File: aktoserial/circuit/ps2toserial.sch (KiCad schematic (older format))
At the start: 14 parts, among them IC1 ATMEGA8-P, P1 CONN_4, SW1 SW_PUSH, X1 16MHz

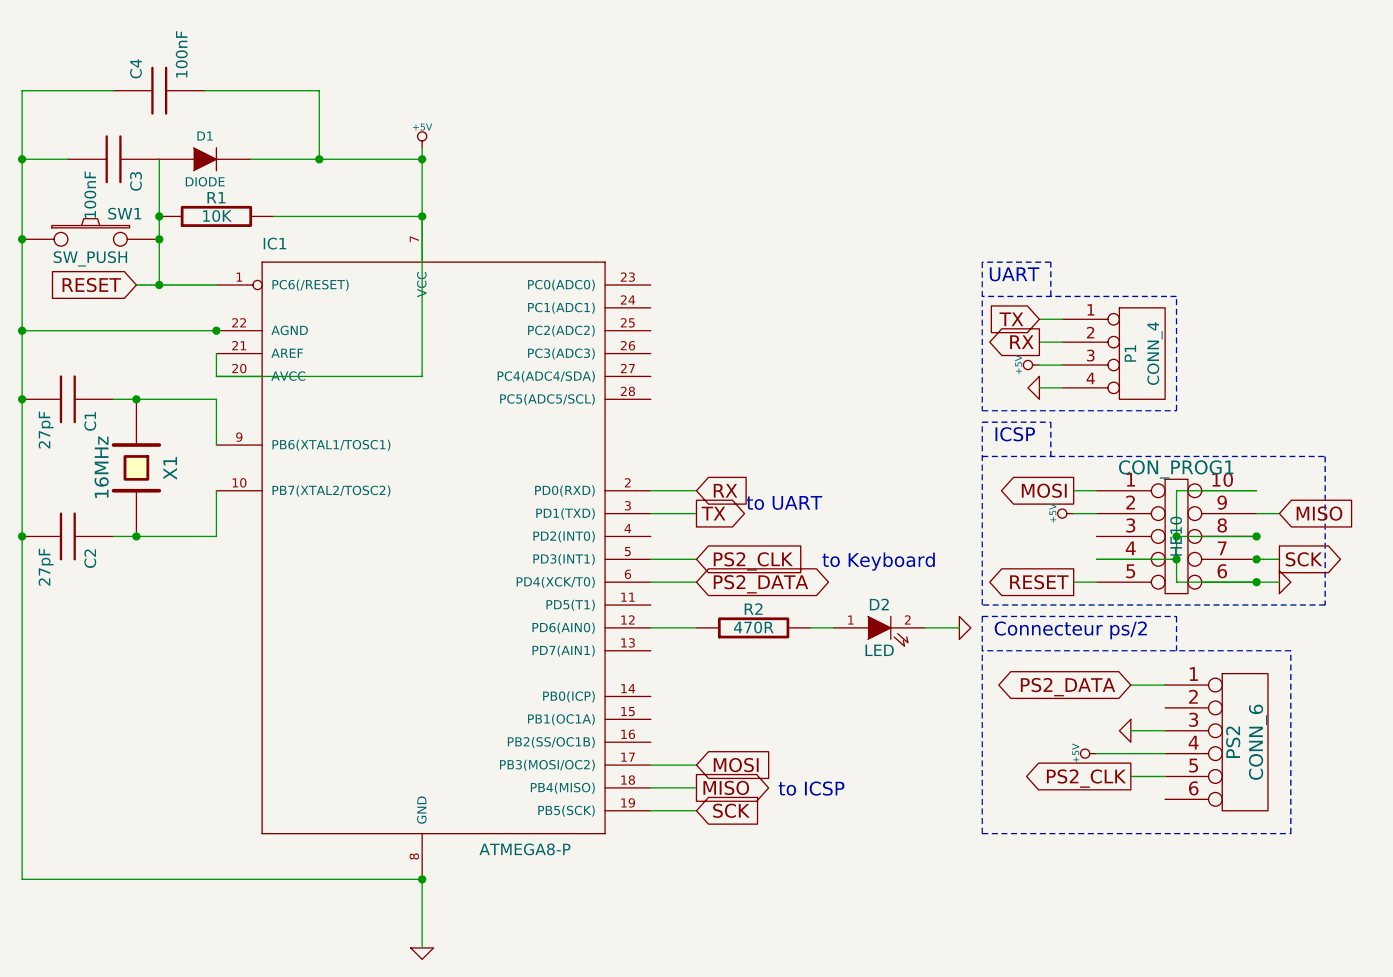
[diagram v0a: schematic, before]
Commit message: * Version finale du circuit aktousb/ps2tousb
git-svn-id: svn://pulkomandy.tk/avrstuff@2 c6672c3c-f6b6-47f9-9001-1fd6b12fecbe
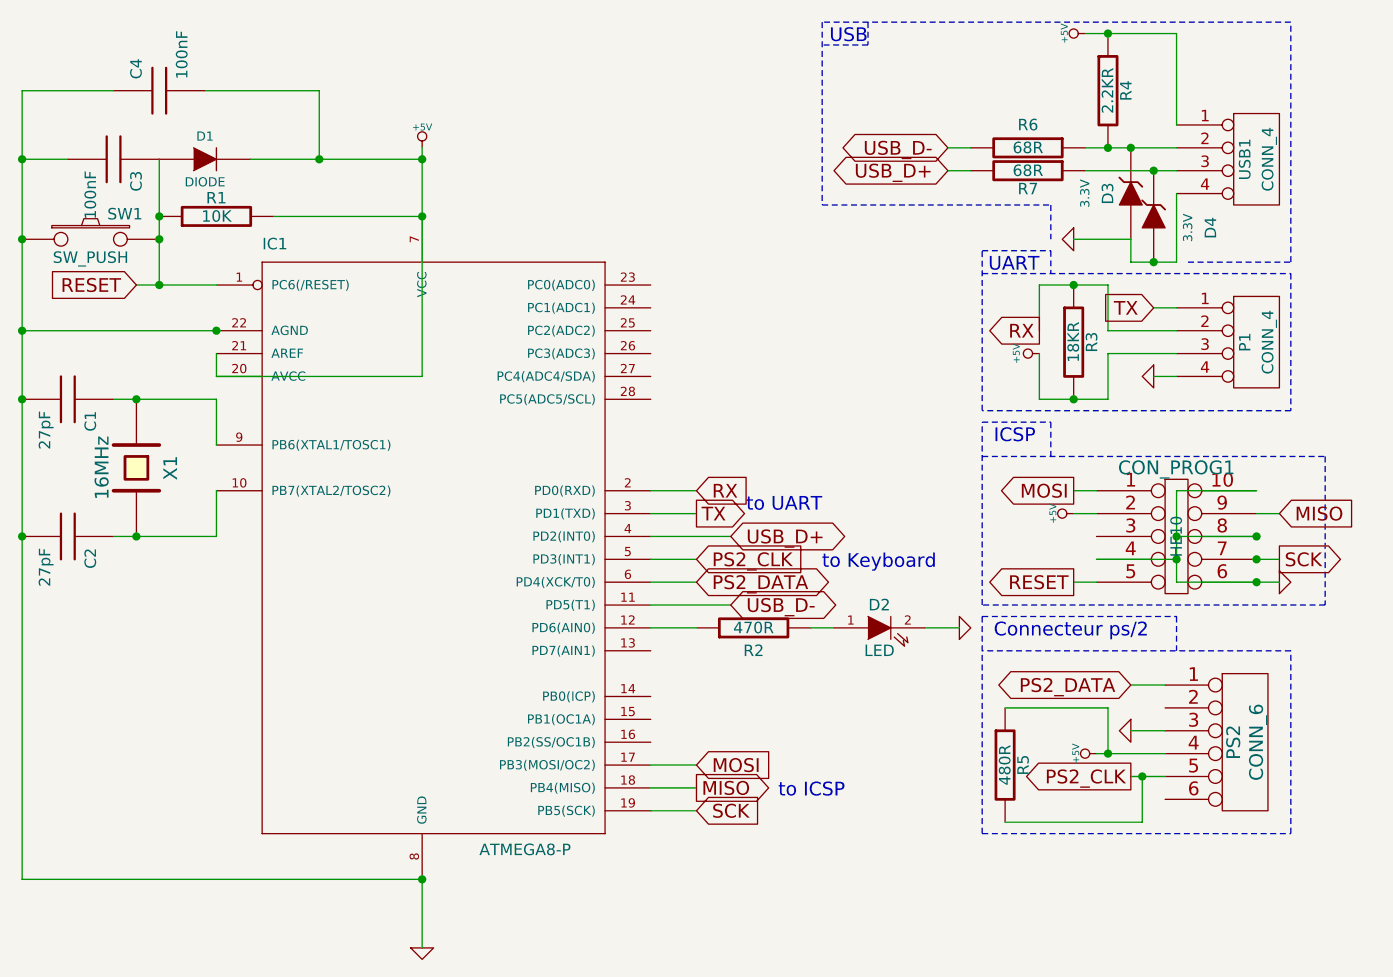
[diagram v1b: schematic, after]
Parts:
- added D3, D4: 3.3V, symbol ZENER
- added R3: 18KR, symbol R
- added R4: 2.2KR, symbol R
- added R5: 480R, symbol R
- added R6, R7: 68R, symbol R
- added USB1: CONN_4, symbol CONN_4
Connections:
- net +5V: now also R3.2, R4.1, R5.1, USB1.1 (P1)
- net GND: now also D3.1 (A), D4.1 (A), USB1.4 (P4)
- net PS2_CLK: now also R5.2
- net RX: now also R3.1
- net USB_D-: now reaches IC1.11 (PD5(T1))
- net USB_D-: now also R6.2
- net USB_D+: now reaches IC1.4 (PD2(INT0))
- net USB_D+: now also R7.2
- new net: D3.2 (K), R4.2, R6.1, USB1.2 (P2)
- new net: D4.2 (K), R7.1, USB1.3 (P3)
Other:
- note added: "USB"
- moved on the sheet: P1

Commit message: Version finale finale du PCB pour commercialisation!
git-svn-id: svn://pulkomandy.tk/avrstuff@3 c6672c3c-f6b6-47f9-9001-1fd6b12fecbe
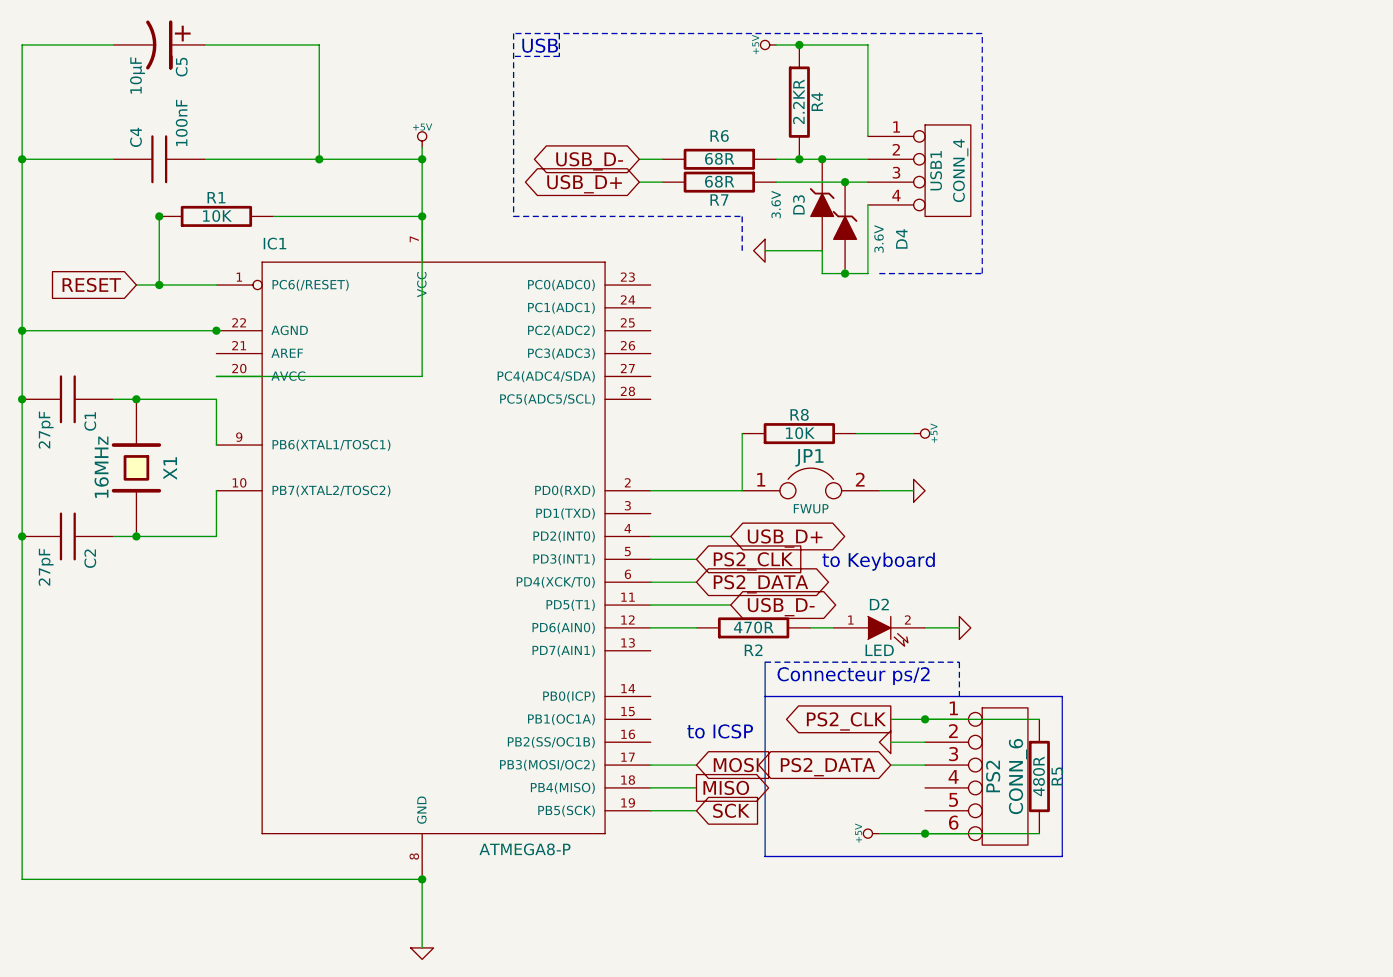
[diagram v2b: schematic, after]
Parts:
- removed C3: 100nF, symbol C
- removed CON_PROG1: HE10, HE10-10d, symbol DIL10
- removed D1: DIODE, symbol DIODE
- removed P1: CONN_4, symbol CONN_4
- removed R3: 18KR, symbol R
- removed SW1: SW_PUSH, symbol SW_PUSH
- added C5: 10µF, symbol CP1
- added JP1: FWUP, symbol JUMPER
- added R8: 10K, symbol R
- D3, D4: value 3.3V -> 3.6V
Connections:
- net +5V: now also PS2.6, R5.2, C5.1, R8.2; no longer IC1.21 (AREF), PS2.4, R5.1
- net GND: now also PS2.2, C5.2, JP1.2; no longer PS2.3
- net PS2_CLK: now also PS2.1, R5.1; no longer PS2.5, R5.2
- net PS2_DATA: now also PS2.3; no longer PS2.1
- net RX: no longer names the net of IC1.2 (PD0(RXD))
- net RX: now also JP1.1, R8.1
- net TX: no longer names the net of IC1.3 (PD1(TXD))
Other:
- note removed: "ICSP"
- note removed: "UART"
- note removed: "to UART"
- moved on the sheet: C4, D3, D4, PS2, R4, R5, R6, R7, USB1
